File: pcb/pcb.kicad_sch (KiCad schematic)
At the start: 23 parts, among them J1 Conn_01x04_MountingPin, J2 Conn_01x04_MountingPin, J4 Conn_ARM_SWD_TagConnect_TC203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, U1 MCP2542FDxMF, U2 STM32G0B1KBUx, U3 MCP1792x-3302xCB

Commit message: unrouted nets 0
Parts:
- C10, C11, C12, C3, C7, C9: footprint (none) -> Capacitor_SMD:C_0402_1005Metric
- C13, C4, C8: footprint (none) -> Capacitor_SMD:C_0603_1608Metric
- J1, J2: footprint (none) -> goatworks-footprint-library:CONN04_5055670471_MOL
- JP1: footprint (none) -> Jumper:SolderJumper-2_P1.3mm_Open_RoundedPad1.0x1.5mm
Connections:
- net CANH: now also J1.4 (Pin_4), J2.4 (Pin_4); no longer J1.3 (Pin_3), J2.3 (Pin_3)
- net CANL: now also J1.3 (Pin_3), J2.3 (Pin_3); no longer J1.4 (Pin_4), J2.4 (Pin_4)
- net GND: no longer M1.3 (CLK), M2.3 (CLK), U2.27 (PB3)
- new net SCL: M1.3 (CLK), M2.3 (CLK), U2.27 (PB3)
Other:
- moved on the sheet: C1, C10, C11, C12, C13, C2, C5, C6, C9, J1, J2, J4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

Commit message: improve routing
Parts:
- removed C5, C6: 1u, Capacitor_SMD:C_0402_1005Metric, symbol Device:C_Small
- removed JP1: SolderJumper_2_Open, Jumper:SolderJumper-2_P1.3mm_Open_RoundedPad1.0x1.5mm, symbol Jumper:SolderJumper_2_Open
- added C14: 4.7u, Capacitor_SMD:C_0603_1608Metric, symbol Device:C_Small
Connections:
- net GND: now also LS1.1
- net SPEAKER: now also C14.1; no longer LS1.2
- new net: C14.2, LS1.2

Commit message: re route!!!
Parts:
- added C15, C16: 100n, Capacitor_SMD:C_0402_1005Metric, symbol Device:C_Small
- added D1: CAN_TVS, Package_TO_SOT_SMD:SOT-23-3, symbol glv:CDSOT23-T24CAN
- added M3, M4: ~, goatworks-footprint-library:T3902, symbol goatworks:T3902
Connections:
- net +3V3: now also C15.2, C16.2, M3.5 (VDD), M4.2 (Select), M4.5 (VDD)
- net GND: now also C15.1, C16.1, D1.3 (Output), M3.2 (Select), M3.3 (GND), M4.3 (GND)
- net I2S_SD: now reaches U2.29 (PB5)
- net I2S_SD: now also M1.4 (DOUT), M2.4 (DOUT), M3.1 (Data), M4.1 (Data)
- net CANH renamed CAN+
- net CAN+: now also D1.2 (Input)
- net CANL renamed CAN-
- net CAN-: now also D1.1 (Input)
- net SCL renamed I2S_CLK
- net I2S_CLK: now also M3.4 (CLK), M4.4 (CLK)
- removed net SDA: M1.4 (DOUT), M2.4 (DOUT), U2.28 (PB4)
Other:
- moved on the sheet: C10, C9, U1

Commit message: T3902 Mic
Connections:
- net SWO: now also U2.19 (PA9/UCPD1_DBCC1)
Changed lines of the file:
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@@
+	(wire
+		(pts
+			(xy 193.04 71.12) (xy 201.93 71.12)
+		)
+		(stroke
+			(width 0)
+			(type default)
+		)
+	)
 	(wire
 		(pts
@@
 		)
 	)
+	(label "SWO"
+		(at 201.93 71.12 180)
+		(effects
+			(font
+				(size 1.27 1.27)
+			)
+			(justify right bottom)
+		)
+	)
 	(label "CAN+"
 		(at 238.76 146.05 0)
@@
 		)
 	)
+	(label "SWO"
+		(at 208.28 146.05 180)
+		(effects
+			(font
+				(size 1.27 1.27)
+			)
+			(justify right bottom)
+		)
+	)
 	(label "SWDIO"
 		(at 201.93 78.74 180)
@@
 		)
 	)
-	(label "SWO"
-		(at 208.28 146.05 180)
-		(effects
-			(font
-				(size 1.27 1.27)
-			)
-			(justify right bottom)
-		)
-	)

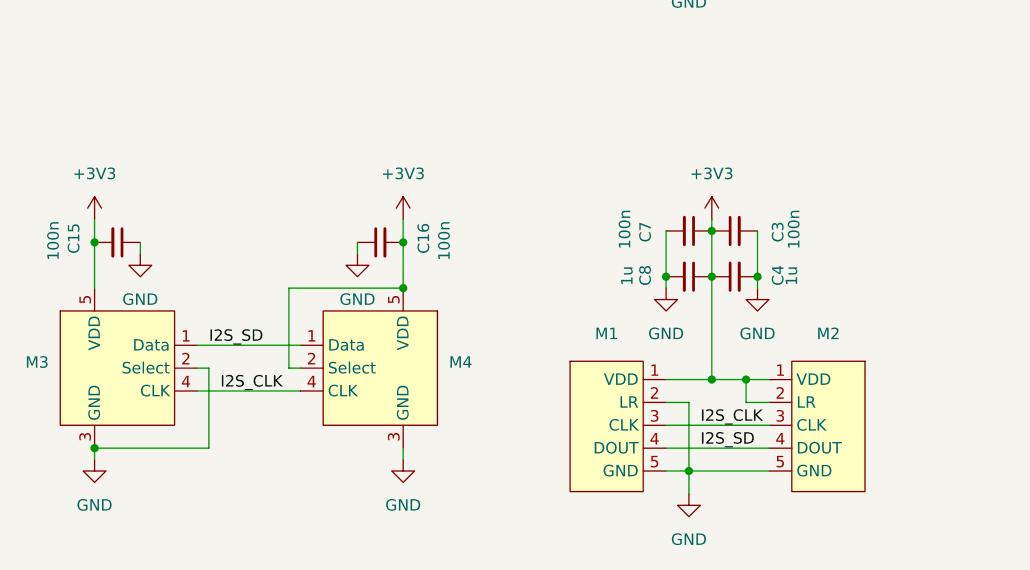
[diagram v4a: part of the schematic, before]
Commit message: add source termination
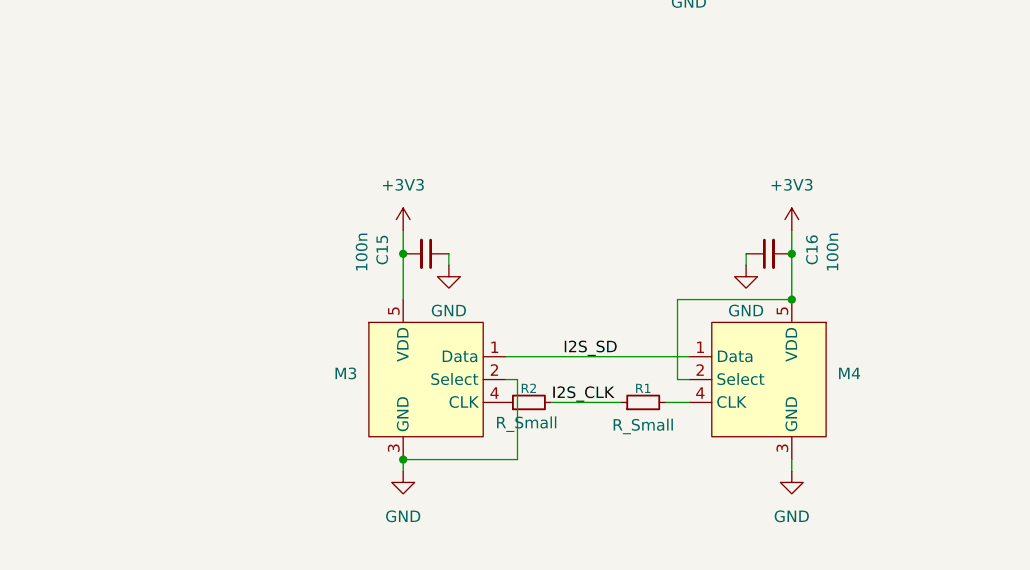
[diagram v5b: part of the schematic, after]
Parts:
- removed C3, C7: 100n, Capacitor_SMD:C_0402_1005Metric, symbol Device:C_Small
- removed C4, C8: 1u, Capacitor_SMD:C_0603_1608Metric, symbol Device:C_Small
- removed M1, M2: ~, goatworks-footprint-library:MP34DT05-A, symbol goatworks:MP34DT05-A
- added R1, R2: R_Small, Resistor_SMD:R_0402_1005Metric, symbol Device:R_Small
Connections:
- net I2S_CLK: now also R1.1, R2.2; no longer M3.4 (CLK), M4.4 (CLK)
- new net: M4.4 (CLK), R1.2
- new net: M3.4 (CLK), R2.1
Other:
- moved on the sheet: C15, C16, M3, M4
